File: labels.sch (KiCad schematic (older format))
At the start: 18 parts

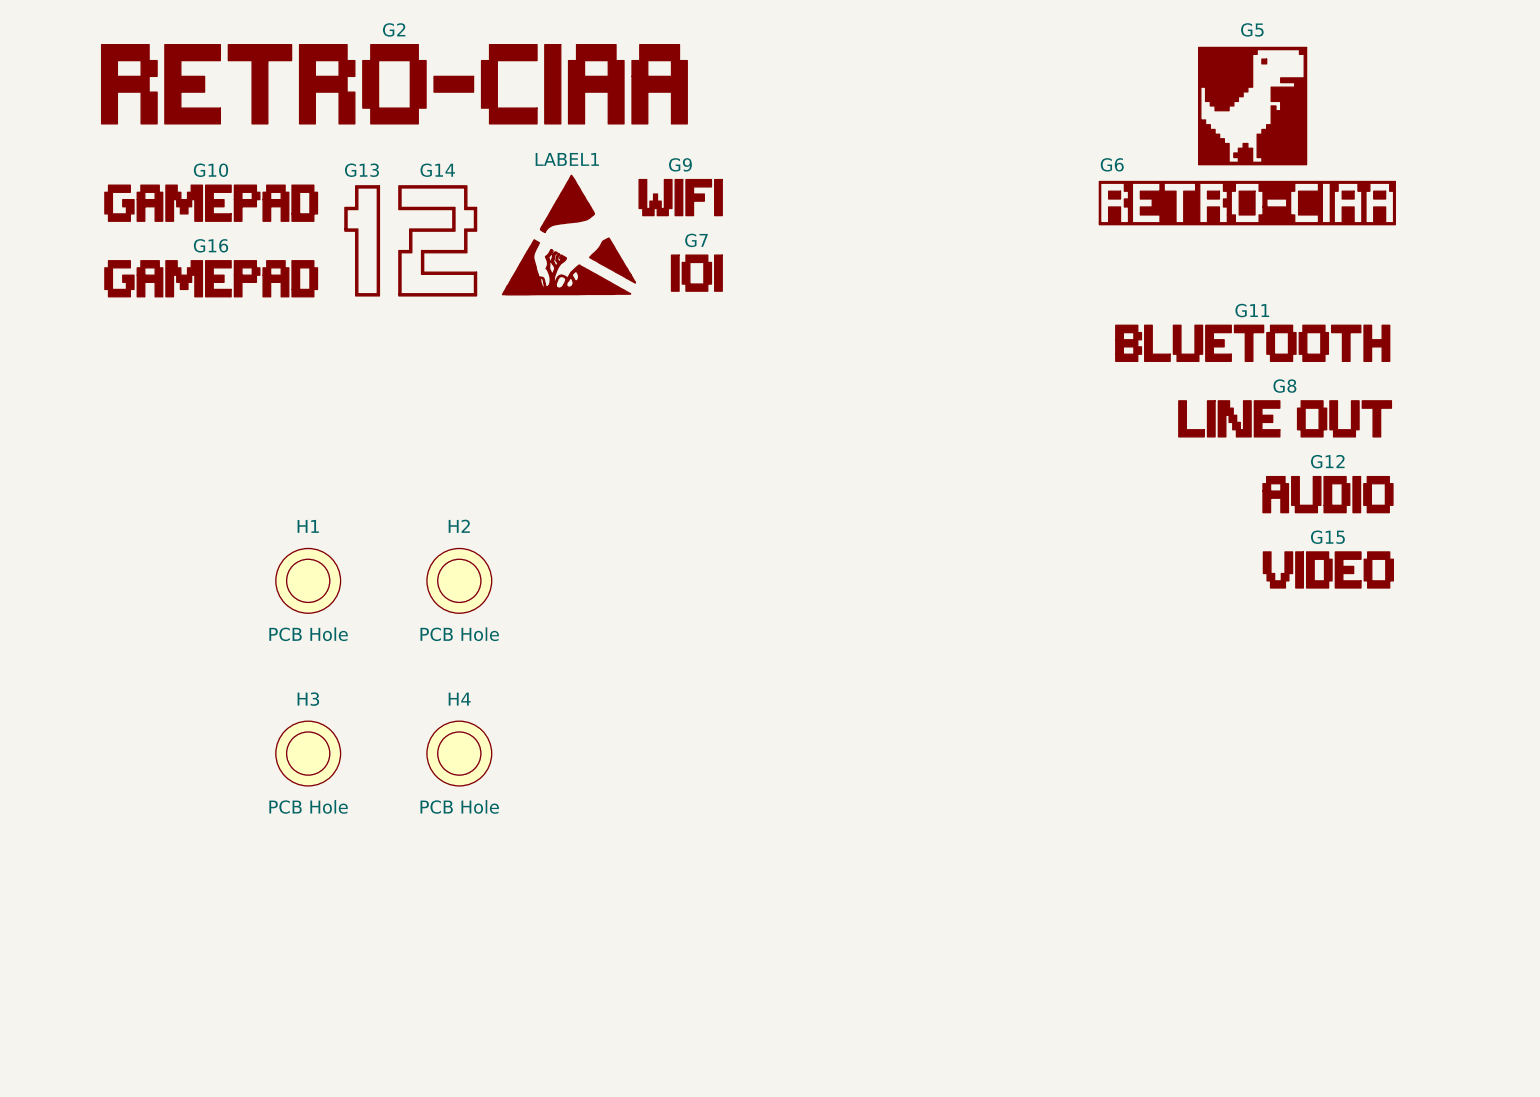
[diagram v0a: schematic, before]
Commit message: Detalles menores (reordenamiento de labels, correccion de titulo, etc
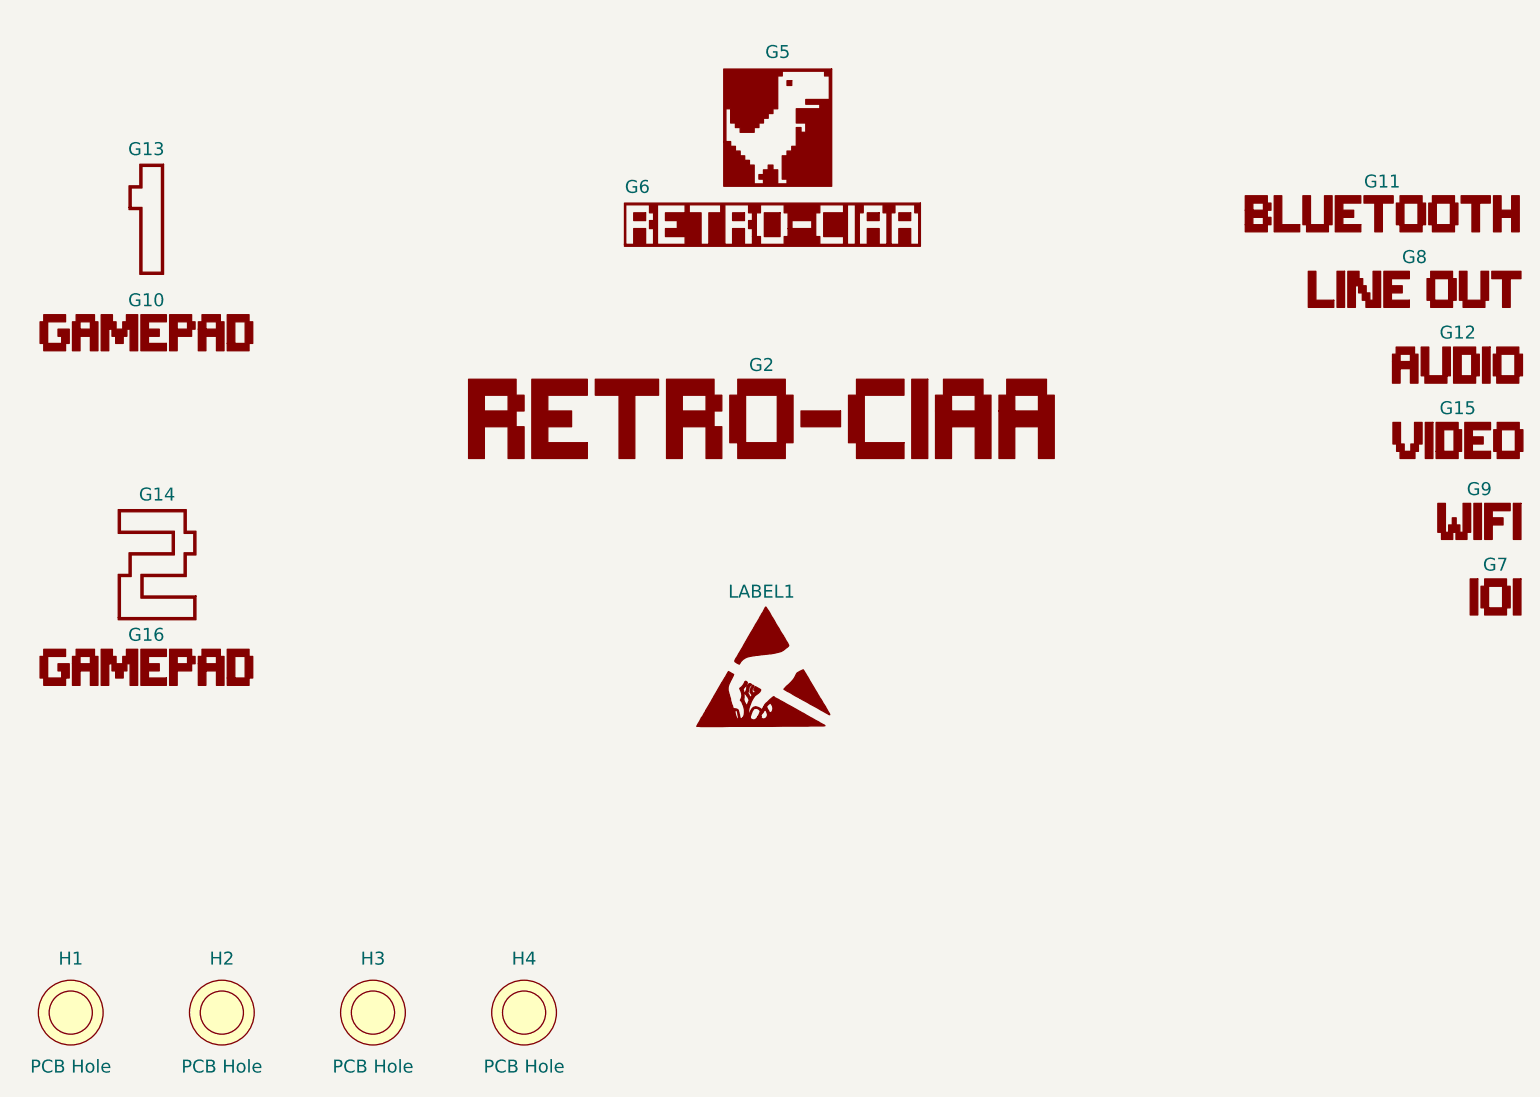
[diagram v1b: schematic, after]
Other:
- moved on the sheet: G10, G11, G12, G13, G14, G15, G16, G2, G5, G6, G7, G8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
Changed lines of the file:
@@
 L PCB_Hole H1
 U 1 1 5BD21399
-P 3700 4700
-F 0 "H1" H 3700 4950 60  0000 C CNN
-F 1 "PCB Hole" H 3700 4450 60  0000 C CNN
-F 2 "Mounting_Holes:MountingHole_3.7mm_Pad_Via" H 3600 4800 60  0001 C CNN
-F 3 "" H 3700 4900 60  0001 C CNN
-	1    3700 4700
+P 2600 6700
+F 0 "H1" H 2600 6950 60  0000 C CNN
+F 1 "PCB Hole" H 2600 6450 60  0000 C CNN
+F 2 "Mounting_Holes:MountingHole_3.7mm_Pad_Via" H 2500 6800 60  0001 C CNN
+F 3 "" H 2600 6900 60  0001 C CNN
+	1    2600 6700
 	1    0    0    -1
 $EndComp
@@
 L PCB_Hole H2
 U 1 1 5BD213A0
-P 4400 4700
-F 0 "H2" H 4400 4950 60  0000 C CNN
-F 1 "PCB Hole" H 4400 4450 60  0000 C CNN
-F 2 "Mounting_Holes:MountingHole_3.7mm_Pad_Via" H 4300 4800 60  0001 C CNN
-F 3 "" H 4400 4900 60  0001 C CNN
-	1    4400 4700
+P 3300 6700
+F 0 "H2" H 3300 6950 60  0000 C CNN
+F 1 "PCB Hole" H 3300 6450 60  0000 C CNN
+F 2 "Mounting_Holes:MountingHole_3.7mm_Pad_Via" H 3200 6800 60  0001 C CNN
+F 3 "" H 3300 6900 60  0001 C CNN
+	1    3300 6700
 	1    0    0    -1
 $EndComp
@@
 L PCB_Hole H3
 U 1 1 5BD213A7
-P 3700 5500
-F 0 "H3" H 3700 5750 60  0000 C CNN
-F 1 "PCB Hole" H 3700 5250 60  0000 C CNN
-F 2 "Mounting_Holes:MountingHole_3.7mm_Pad_Via" H 3600 5600 60  0001 C CNN
-F 3 "" H 3700 5700 60  0001 C CNN
-	1    3700 5500
+P 4000 6700
+F 0 "H3" H 4000 6950 60  0000 C CNN
+F 1 "PCB Hole" H 4000 6450 60  0000 C CNN
+F 2 "Mounting_Holes:MountingHole_3.7mm_Pad_Via" H 3900 6800 60  0001 C CNN
+F 3 "" H 4000 6900 60  0001 C CNN
+	1    4000 6700
 	1    0    0    -1
 $EndComp
@@
 L PCB_Hole H4
 U 1 1 5BD213AE
-P 4400 5500
-F 0 "H4" H 4400 5750 60  0000 C CNN
-F 1 "PCB Hole" H 4400 5250 60  0000 C CNN
-F 2 "Mounting_Holes:MountingHole_3.7mm_Pad_Via" H 4300 5600 60  0001 C CNN
-F 3 "" H 4400 5700 60  0001 C CNN
-	1    4400 5500
+P 4700 6700
+F 0 "H4" H 4700 6950 60  0000 C CNN
+F 1 "PCB Hole" H 4700 6450 60  0000 C CNN
+F 2 "Mounting_Holes:MountingHole_3.7mm_Pad_Via" H 4600 6800 60  0001 C CNN
+F 3 "" H 4700 6900 60  0001 C CNN
+	1    4700 6700
 	1    0    0    -1
 $EndComp
@@
 L ESD_LOGO_15 LABEL1
 U 1 1 5BD213B5
-P 4900 3100
-F 0 "LABEL1" H 4900 3450 60  0000 C CNN
-F 1 "ESD_LOGO_15" H 4900 3388 60  0001 C CNN
-F 2 "Salmon:ESD_Sign_12" H 4900 3100 60  0001 C CNN
-F 3 "" H 4900 3100 60  0000 C CNN
-	1    4900 3100
+P 5800 5100
+F 0 "LABEL1" H 5800 5450 60  0000 C CNN
+F 1 "ESD_LOGO_15" H 5800 5388 60  0001 C CNN
+F 2 "Salmon:ESD_Sign_12" H 5800 5100 60  0001 C CNN
+F 3 "" H 5800 5100 60  0000 C CNN
+	1    5800 5100
 	1    0    0    -1
 $EndComp
@@
 L RETROCIAA_LOGO G2
 U 1 1 5BD213BC
-P 4100 2400
-F 0 "G2" H 4100 2650 60  0000 C CNN
-F 1 "RETROCIAA_LOGO" H 4100 2586 60  0001 C CNN
-F 2 "Salmon:RETROCIAA_LOGO" H 4100 2400 60  0001 C CNN
-F 3 "" H 4100 2400 60  0001 C CNN
-	1    4100 2400
+P 5800 3950
+F 0 "G2" H 5800 4200 60  0000 C CNN
+F 1 "RETROCIAA_LOGO" H 5800 4136 60  0001 C CNN
+F 2 "Salmon:RETROCIAA_LOGO" H 5800 3950 60  0001 C CNN
+F 3 "" H 5800 3950 60  0001 C CNN
+	1    5800 3950
 	1    0    0    -1
 $EndComp
@@
 L RETROCIAA_LOGO_FRONT G6
 U 1 1 5BD213C3
-P 8050 2950
-F 0 "G6" H 7425 3125 60  0000 C CNN
-F 1 "RETROCIAA_LOGO_FRONT" H 8050 2800 60  0001 C CNN
-F 2 "Salmon:RETROCIAA_LOGO_FRONT" H 8050 2950 60  0001 C CNN
-F 3 "" H 8050 2950 60  0001 C CNN
-	1    8050 2950
+P 5850 3050
+F 0 "G6" H 5225 3225 60  0000 C CNN
+F 1 "RETROCIAA_LOGO_FRONT" H 5850 2900 60  0001 C CNN
+F 2 "Salmon:RETROCIAA_LOGO_FRONT" H 5850 3050 60  0001 C CNN
+F 3 "" H 5850 3050 60  0001 C CNN
+	1    5850 3050
 	1    0    0    -1
 $EndComp
@@
 L TREX_LOGO_FRONT G5
 U 1 1 5BD213CA
-P 8075 2500
-F 0 "G5" H 8075 2850 60  0000 C CNN
-F 1 "LOGO_FRONT" H 8075 2250 60  0001 C CNN
-F 2 "Salmon:TREX_LOGO_FRONT" H 8075 2500 60  0001 C CNN
-F 3 "" H 8075 2500 60  0001 C CNN
-	1    8075 2500
+P 5875 2600
+F 0 "G5" H 5875 2950 60  0000 C CNN
+F 1 "LOGO_FRONT" H 5875 2350 60  0001 C CNN
+F 2 "Salmon:TREX_LOGO_FRONT" H 5875 2600 60  0001 C CNN
+F 3 "" H 5875 2600 60  0001 C CNN
+	1    5875 2600
 	1    0    0    -1
 $EndComp
@@
 L RETROCIAA_1 G13
 U 1 1 5BD213D1
-P 3950 3125
-F 0 "G13" H 3950 3450 60  0000 C CNN
-F 1 "RETROCIAA_1" H 3950 3355 60  0001 C CNN
-F 2 "Salmon:RETROCIAA_1" H 3950 3125 60  0001 C CNN
-F 3 "" H 3950 3125 60  0001 C CNN
-	1    3950 3125
+P 2950 3025
+F 0 "G13" H 2950 3350 60  0000 C CNN
+F 1 "RETROCIAA_1" H 2950 3255 60  0001 C CNN
+F 2 "Salmon:RETROCIAA_1" H 2950 3025 60  0001 C CNN
+F 3 "" H 2950 3025 60  0001 C CNN
+	1    2950 3025
 	1    0    0    -1
 $EndComp
@@
 L RETROCIAA_2 G14
 U 1 1 5BD213D8
-P 4300 3125
-F 0 "G14" H 4300 3450 60  0000 C CNN
-F 1 "RETROCIAA_2" H 4300 3355 60  0001 C CNN
-F 2 "Salmon:RETROCIAA_2" H 4300 3125 60  0001 C CNN
-F 3 "" H 4300 3125 60  0001 C CNN
-	1    4300 3125
+P 3000 4625
+F 0 "G14" H 3000 4950 60  0000 C CNN
+F 1 "RETROCIAA_2" H 3000 4855 60  0001 C CNN
+F 2 "Salmon:RETROCIAA_2" H 3000 4625 60  0001 C CNN
+F 3 "" H 3000 4625 60  0001 C CNN
+	1    3000 4625
 	1    0    0    -1
 $EndComp
@@
 L RETROCIAA_AUDIO G12
 U 1 1 5BD213DF
-P 8425 4300
-F 0 "G12" H 8425 4450 60  0000 C CNN
-F 1 "RETROCIAA_AUDIO" H 8425 4361 60  0001 C CNN
-F 2 "Salmon:RETROCIAA_AUDIO" H 8425 4300 60  0001 C CNN
-F 3 "" H 8425 4300 60  0001 C CNN
-	1    8425 4300
+P 9025 3700
+F 0 "G12" H 9025 3850 60  0000 C CNN
+F 1 "RETROCIAA_AUDIO" H 9025 3761 60  0001 C CNN
+F 2 "Salmon:RETROCIAA_AUDIO" H 9025 3700 60  0001 C CNN
+F 3 "" H 9025 3700 60  0001 C CNN
+	1    9025 3700
 	1    0    0    -1
 $EndComp
@@
 L RETROCIAA_BLUETOOTH G11
 U 1 1 5BD213E6
-P 8075 3600
-F 0 "G11" H 8075 3750 60  0000 C CNN
-F 1 "RETROCIAA_BLUETOOTH" H 8075 3660 60  0001 C CNN
-F 2 "Salmon:RETROCIAA_BLUETOOTH" H 8075 3600 60  0001 C CNN
-F 3 "" H 8075 3600 60  0001 C CNN
-	1    8075 3600
+P 8675 3000
+F 0 "G11" H 8675 3150 60  0000 C CNN
+F 1 "RETROCIAA_BLUETOOTH" H 8675 3060 60  0001 C CNN
+F 2 "Salmon:RETROCIAA_BLUETOOTH" H 8675 3000 60  0001 C CNN
+F 3 "" H 8675 3000 60  0001 C CNN
+	1    8675 3000
 	1    0    0    -1
 $EndComp
@@
 L RETROCIAA_GAMEPAD G10
 U 1 1 5BD213ED
-P 3250 2950
-F 0 "G10" H 3250 3100 60  0000 C CNN
-F 1 "RETROCIAA_GAMEPAD" H 3250 3011 60  0001 C CNN
-F 2 "Salmon:RETROCIAA_GAMEPAD" H 3250 2950 60  0001 C CNN
-F 3 "" H 3250 2950 60  0001 C CNN
-	1    3250 2950
+P 2950 3550
+F 0 "G10" H 2950 3700 60  0000 C CNN
+F 1 "RETROCIAA_GAMEPAD" H 2950 3611 60  0001 C CNN
+F 2 "Salmon:RETROCIAA_GAMEPAD" H 2950 3550 60  0001 C CNN
+F 3 "" H 2950 3550 60  0001 C CNN
+	1    2950 3550
 	1    0    0    -1
 $EndComp
@@
 L RETROCIAA_LINEOUT G8
 U 1 1 5BD213F4
-P 8225 3950
-F 0 "G8" H 8225 4100 60  0000 C CNN
-F 1 "RETROCIAA_LINEOUT" H 8225 4010 60  0001 C CNN
-F 2 "Salmon:RETROCIAA_LINEOUT" H 8225 3950 60  0001 C CNN
-F 3 "" H 8225 3950 60  0001 C CNN
-	1    8225 3950
+P 8825 3350
+F 0 "G8" H 8825 3500 60  0000 C CNN
+F 1 "RETROCIAA_LINEOUT" H 8825 3410 60  0001 C CNN
+F 2 "Salmon:RETROCIAA_LINEOUT" H 8825 3350 60  0001 C CNN
+F 3 "" H 8825 3350 60  0001 C CNN
+	1    8825 3350
 	1    0    0    -1
 $EndComp
@@
 L RETROCIAA_VIDEO G15
 U 1 1 5BD213FB
-P 8425 4650
-F 0 "G15" H 8425 4800 60  0000 C CNN
-F 1 "RETROCIAA_VIDEO" H 8425 4710 60  0001 C CNN
-F 2 "Salmon:RETROCIAA_VIDEO" H 8425 4650 60  0001 C CNN
-F 3 "" H 8425 4650 60  0001 C CNN
-	1    8425 4650
+P 9025 4050
+F 0 "G15" H 9025 4200 60  0000 C CNN
+F 1 "RETROCIAA_VIDEO" H 9025 4110 60  0001 C CNN
+F 2 "Salmon:RETROCIAA_VIDEO" H 9025 4050 60  0001 C CNN
+F 3 "" H 9025 4050 60  0001 C CNN
+	1    9025 4050
 	1    0    0    -1
 $EndComp
@@
 L RETROCIAA_VIDEO_CONN G7
 U 1 1 5BD21402
-P 5500 3275
-F 0 "G7" H 5500 3425 60  0000 C CNN
-F 1 "RETROCIAA_VIDEO_CONN" H 5500 3335 60  0001 C CNN
-F 2 "Salmon:RETROCIAA_VIDEO_CONN" H 5500 3275 60  0001 C CNN
-F 3 "" H 5500 3275 60  0001 C CNN
-	1    5500 3275
+P 9200 4775
+F 0 "G7" H 9200 4925 60  0000 C CNN
+F 1 "RETROCIAA_VIDEO_CONN" H 9200 4835 60  0001 C CNN
+F 2 "Salmon:RETROCIAA_VIDEO_CONN" H 9200 4775 60  0001 C CNN
+F 3 "" H 9200 4775 60  0001 C CNN
+	1    9200 4775
 	1    0    0    -1
 $EndComp
@@
 L RETROCIAA_WIFI G9
 U 1 1 5BD21409
-P 5425 2925
-F 0 "G9" H 5425 3075 60  0000 C CNN
-F 1 "RETROCIAA_WIFI" H 5425 2985 60  0001 C CNN
-F 2 "Salmon:RETROCIAA_WIFI" H 5425 2925 60  0001 C CNN
-F 3 "" H 5425 2925 60  0001 C CNN
-	1    5425 2925
+P 9125 4425
+F 0 "G9" H 9125 4575 60  0000 C CNN
+F 1 "RETROCIAA_WIFI" H 9125 4485 60  0001 C CNN
+F 2 "Salmon:RETROCIAA_WIFI" H 9125 4425 60  0001 C CNN
+F 3 "" H 9125 4425 60  0001 C CNN
+	1    9125 4425
 	1    0    0    -1
 $EndComp
@@
 L RETROCIAA_GAMEPAD G16
 U 1 1 5BD21410
-P 3250 3300
-F 0 "G16" H 3250 3450 60  0000 C CNN
-F 1 "RETROCIAA_GAMEPAD" H 3250 3361 60  0001 C CNN
-F 2 "Salmon:RETROCIAA_GAMEPAD" H 3250 3300 60  0001 C CNN
-F 3 "" H 3250 3300 60  0001 C CNN
-	1    3250 3300
+P 2950 5100
+F 0 "G16" H 2950 5250 60  0000 C CNN
+F 1 "RETROCIAA_GAMEPAD" H 2950 5161 60  0001 C CNN
+F 2 "Salmon:RETROCIAA_GAMEPAD" H 2950 5100 60  0001 C CNN
+F 3 "" H 2950 5100 60  0001 C CNN
+	1    2950 5100
 	1    0    0    -1
 $EndComp

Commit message: Cambios menores
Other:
- moved on the sheet: G10, G13, G14, G16, G5, G6
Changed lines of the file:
@@
 Comment1 "All resistors 1% & 0603\" unless otherwise noted"
 Comment2 "ERC check OK on 2018-10-19"
-Comment3 ""
+Comment3 "T-Rex image by Chromium Project, Sebastien Gabriel."
 Comment4 "Copyright 2018 Santiago Germino (see LICENSE)"
 $EndDescr
@@
 L RETROCIAA_LOGO_FRONT G6
 U 1 1 5BD213C3
-P 5850 3050
-F 0 "G6" H 5225 3225 60  0000 C CNN
-F 1 "RETROCIAA_LOGO_FRONT" H 5850 2900 60  0001 C CNN
-F 2 "Salmon:RETROCIAA_LOGO_FRONT" H 5850 3050 60  0001 C CNN
-F 3 "" H 5850 3050 60  0001 C CNN
-	1    5850 3050
+P 5750 3050
+F 0 "G6" H 5125 3225 60  0000 C CNN
+F 1 "RETROCIAA_LOGO_FRONT" H 5750 2900 60  0001 C CNN
+F 2 "Salmon:RETROCIAA_LOGO_FRONT" H 5750 3050 60  0001 C CNN
+F 3 "" H 5750 3050 60  0001 C CNN
+	1    5750 3050
 	1    0    0    -1
 $EndComp
@@
 L TREX_LOGO_FRONT G5
 U 1 1 5BD213CA
-P 5875 2600
-F 0 "G5" H 5875 2950 60  0000 C CNN
-F 1 "LOGO_FRONT" H 5875 2350 60  0001 C CNN
-F 2 "Salmon:TREX_LOGO_FRONT" H 5875 2600 60  0001 C CNN
-F 3 "" H 5875 2600 60  0001 C CNN
-	1    5875 2600
+P 5775 2600
+F 0 "G5" H 5775 2950 60  0000 C CNN
+F 1 "LOGO_FRONT" H 5775 2350 60  0001 C CNN
+F 2 "Salmon:TREX_LOGO_FRONT" H 5775 2600 60  0001 C CNN
+F 3 "" H 5775 2600 60  0001 C CNN
+	1    5775 2600
 	1    0    0    -1
 $EndComp
@@
 L RETROCIAA_1 G13
 U 1 1 5BD213D1
-P 2950 3025
-F 0 "G13" H 2950 3350 60  0000 C CNN
-F 1 "RETROCIAA_1" H 2950 3255 60  0001 C CNN
-F 2 "Salmon:RETROCIAA_1" H 2950 3025 60  0001 C CNN
-F 3 "" H 2950 3025 60  0001 C CNN
-	1    2950 3025
+P 2950 2925
+F 0 "G13" H 2950 3250 60  0000 C CNN
+F 1 "RETROCIAA_1" H 2950 3155 60  0001 C CNN
+F 2 "Salmon:RETROCIAA_1" H 2950 2925 60  0001 C CNN
+F 3 "" H 2950 2925 60  0001 C CNN
+	1    2950 2925
 	1    0    0    -1
 $EndComp
@@
 L RETROCIAA_2 G14
 U 1 1 5BD213D8
-P 3000 4625
-F 0 "G14" H 3000 4950 60  0000 C CNN
-F 1 "RETROCIAA_2" H 3000 4855 60  0001 C CNN
-F 2 "Salmon:RETROCIAA_2" H 3000 4625 60  0001 C CNN
-F 3 "" H 3000 4625 60  0001 C CNN
-	1    3000 4625
+P 3000 4525
+F 0 "G14" H 3000 4850 60  0000 C CNN
+F 1 "RETROCIAA_2" H 3000 4755 60  0001 C CNN
+F 2 "Salmon:RETROCIAA_2" H 3000 4525 60  0001 C CNN
+F 3 "" H 3000 4525 60  0001 C CNN
+	1    3000 4525
 	1    0    0    -1
 $EndComp
@@
 L RETROCIAA_GAMEPAD G10
 U 1 1 5BD213ED
-P 2950 3550
-F 0 "G10" H 2950 3700 60  0000 C CNN
-F 1 "RETROCIAA_GAMEPAD" H 2950 3611 60  0001 C CNN
-F 2 "Salmon:RETROCIAA_GAMEPAD" H 2950 3550 60  0001 C CNN
-F 3 "" H 2950 3550 60  0001 C CNN
-	1    2950 3550
+P 2950 3450
+F 0 "G10" H 2950 3600 60  0000 C CNN
+F 1 "RETROCIAA_GAMEPAD" H 2950 3511 60  0001 C CNN
+F 2 "Salmon:RETROCIAA_GAMEPAD" H 2950 3450 60  0001 C CNN
+F 3 "" H 2950 3450 60  0001 C CNN
+	1    2950 3450
 	1    0    0    -1
 $EndComp
@@
 L RETROCIAA_GAMEPAD G16
 U 1 1 5BD21410
-P 2950 5100
-F 0 "G16" H 2950 5250 60  0000 C CNN
-F 1 "RETROCIAA_GAMEPAD" H 2950 5161 60  0001 C CNN
-F 2 "Salmon:RETROCIAA_GAMEPAD" H 2950 5100 60  0001 C CNN
-F 3 "" H 2950 5100 60  0001 C CNN
-	1    2950 5100
-	1    0    0    -1
-$EndComp
+P 2950 5000
+F 0 "G16" H 2950 5150 60  0000 C CNN
+F 1 "RETROCIAA_GAMEPAD" H 2950 5061 60  0001 C CNN
+F 2 "Salmon:RETROCIAA_GAMEPAD" H 2950 5000 60  0001 C CNN
+F 3 "" H 2950 5000 60  0001 C CNN
+	1    2950 5000
+	1    0    0    -1
+$EndComp
